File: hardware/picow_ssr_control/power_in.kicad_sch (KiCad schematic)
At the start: 11 parts, among them Q1 IRF4905PBF, Q2 DMG2301L

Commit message: Updated schemas
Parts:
- removed Q2: DMG2301L, Package_TO_SOT_SMD:SOT-23, symbol dragon_mobile:DMG2301L
- REG1: footprint SOT230P700X180-4N -> Package_TO_SOT_SMD:SOT-223; Manufacturer_Name (none) -> Texas Instruments; Manufacturer_Part_Number (none) -> LM7805MPX/NOPB
- RZ1: footprint Resistor_SMD:R_0805_2012Metric -> Resistor_SMD:R_0603_1608Metric
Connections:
- net +VDC renamed VDC
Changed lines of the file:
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@@
   (paper "USLetter")
   (title_block
-    (date "2023-01-27")
+    (date "2023-01-28")
     (rev "0.0.10")
     (comment 2 "http://creativecommons.org/licenses/by-sa/4.0/")

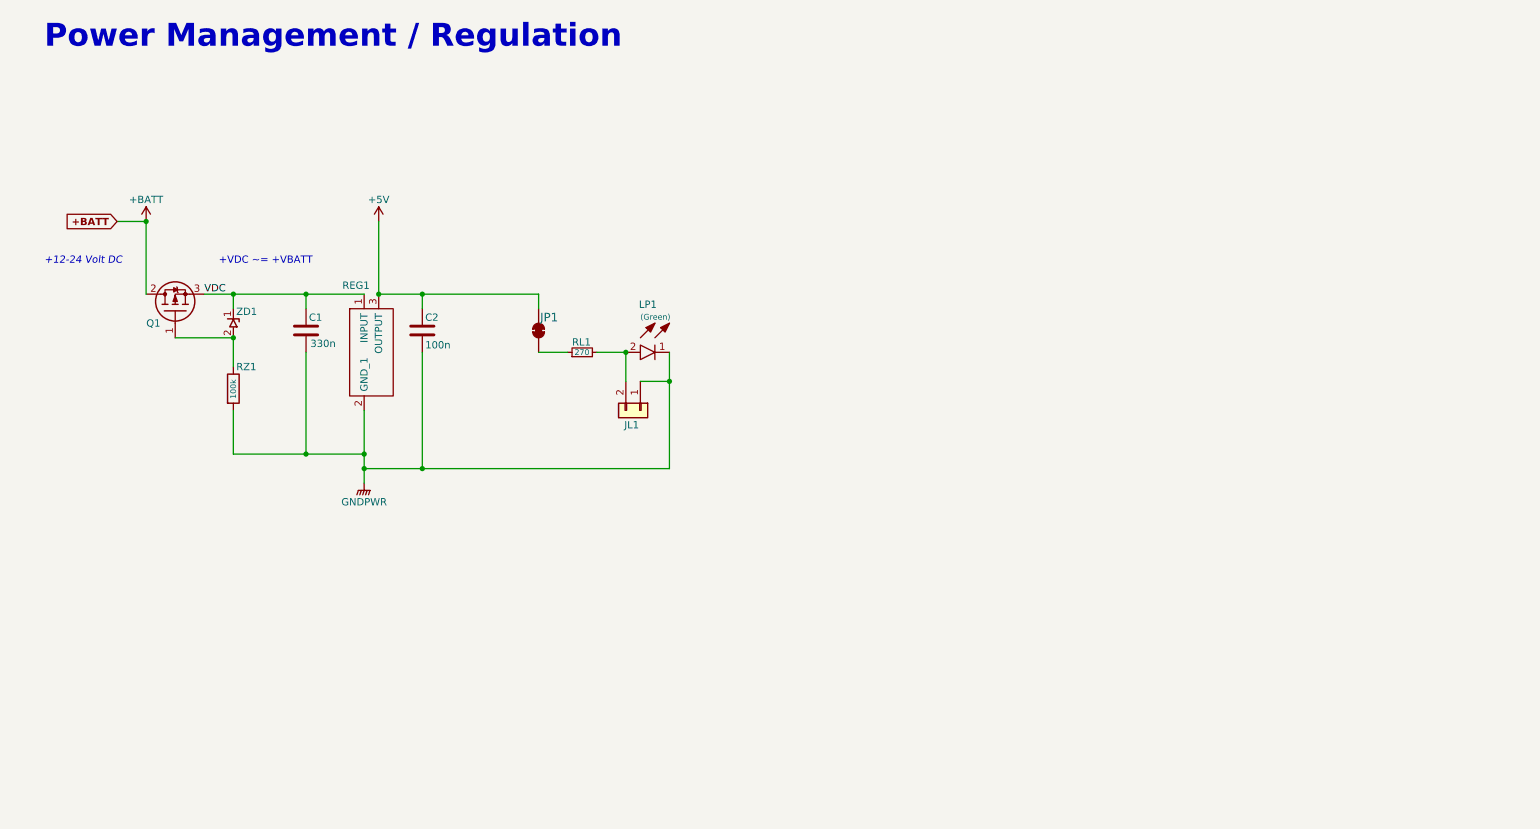
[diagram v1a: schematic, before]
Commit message: Power supply changes plus misc.
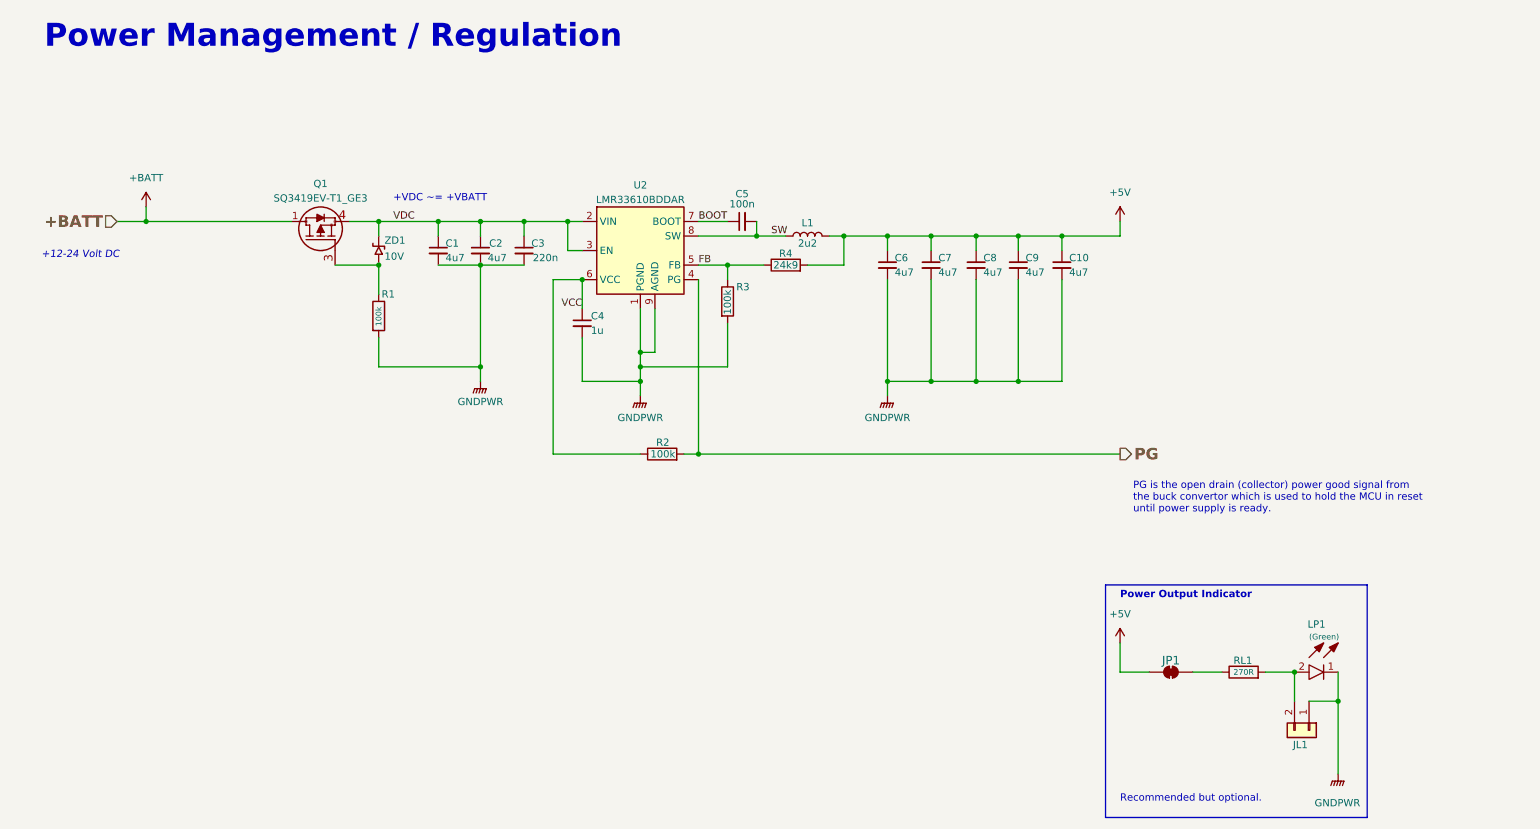
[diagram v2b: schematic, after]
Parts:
- removed C1: 330n, Capacitor_SMD:C_0805_2012Metric, symbol Device:C
- removed C2: 100n, Capacitor_SMD:C_0805_2012Metric, symbol Device:C
- removed Q1: IRF4905PBF, dragon_mobile:TO254P469X1042X1967-3P, symbol dragon_mobile:IRF4905PBF
- removed REG1: LM7805, Package_TO_SOT_SMD:SOT-223, symbol dragon_mobile:LM7805MPX_NOPB
- removed RL1: 270, Resistor_SMD:R_0603_1608Metric, symbol Device:R_Small
- removed RZ1: 100k, Resistor_SMD:R_0603_1608Metric, symbol Device:R
- removed ZD1: +10v Zener Diode, dragon_mobile:BZD27C10P-M3-08, symbol dragon_mobile:BZD27C10P-M3-08
- added C1, C10, C2, C6, C7, C8, C9: 4u7, Capacitor_SMD:C_0805_2012Metric, symbol Device:C_Small
- added C3: 220n, Capacitor_SMD:C_0603_1608Metric, symbol Device:C_Small
- added C4: 1u, Capacitor_SMD:C_0603_1608Metric, symbol Device:C_Small
- added C5: 100n, Capacitor_SMD:C_0603_1608Metric, symbol Device:C_Small
- added L1: 2u2, Inductor_SMD:L_1008_2520Metric, symbol Device:L
- added Q1: SQ3419EV-T1_GE3, dragon_mobile:SOT95P284X110-6N, symbol dragon_mobile:SQ3419EV-T1_BE3
- added R1, R2, R3: 100k, Resistor_SMD:R_0603_1608Metric, symbol Device:R
- added R4: 24k9, Resistor_SMD:R_0603_1608Metric, symbol Device:R
- added RL1: 270R, Resistor_SMD:R_0603_1608Metric, symbol Device:R
- added U2: LMR33610BDDAR, Package_SO:Texas_HSOP-8-1EP_3.9x4.9mm_P1.27mm_ThermalVias, symbol Regulator_Switching:LMR33610BDDAR
- added ZD1: 10V, Diode_SMD:D_0805_2012Metric, symbol dragon_mobile:TSZU52C10
- JL1: footprint Connector_PinHeader_1.00mm:PinHeader_1x02_P1.00mm_Vertical -> dragon_mobile:PinHeader_1x02_P1.00mm_Vertical; Characteristics (none) -> Pin Header; 1mm 1x2 Vertical
- LP1: Manufacturer_Name Lite-On -> (none); Manufacturer_Part_Number LTST-C190KGKT -> (none)
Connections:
- net +5V: now also C10.1, C6.1, C7.1, C8.1, C9.1, L1.2, R4.2
- net +BATT: now also Q1.1 (D), Q1.2 (D), Q1.5 (D), Q1.6 (D)
- net GNDPWR: now also C1.2, C10.2, C2.2, C3.2, C4.2, C6.2, C7.2, C8.2, C9.2, R1.2, R3.2, U2.1 (PGND), U2.9 (AGND)
- net VDC: now also C1.1, C2.1, C3.1, Q1.4 (S), U2.2 (VIN), U2.3 (EN), ZD1.1
- net at JP1.2 (B): now also RL1.1
- net at JL1.2 (Pin_2), LP1.2: now also RL1.2
- new net: Q1.3 (G), R1.1, ZD1.2
- new net BOOT: C5.1, U2.7 (BOOT)
- new net FB: R3.1, R4.1, U2.5 (FB)
- new net PG: R2.2, U2.4 (PG)
- new net SW: C5.2, L1.1, U2.8 (SW)
- new net VCC: C4.1, R2.1, U2.6 (VCC)
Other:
- note added: "PG is the open drain (collector) power good signal from the buck convertor which is used to hold the MCU in reset until power supply is ready."
- note added: "Power Output Indicator"
- note added: "Recommended but optional."

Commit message: Commit before trying changes to power system
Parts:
- LP1: Height 0.8 -> (none)

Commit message: Commit before removing git submodule
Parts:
- added C1: 4u7, Capacitor_SMD:C_0805_2012Metric, symbol Device:C_Small
- added JP1: SolderJumper_2_Bridged, Jumper:SolderJumper-2_P1.3mm_Bridged_RoundedPad1.0x1.5mm, symbol dragon_mobile:SolderJumper_2_Bridged_PowerIn
- added JP2: SolderJumper_2_Open, Jumper:SolderJumper-2_P1.3mm_Open_RoundedPad1.0x1.5mm, symbol Jumper:SolderJumper_2_Open
- added JP3: Conn_01x02, dragon_mobile:PinHeader_1x02_P1.00mm_Vertical, symbol Connector_Generic:Conn_01x02
- L1: symbol Device:L -> dragon_mobile:TFM252012ALVA2R2MTAA
- renumbered C9 to C10, C10 to C11, C1 to C2, C2 to C3, C3 to C4, C4 to C5, C5 to C6, C6 to C7, C7 to C8, C8 to C9, JP1 to JL1, JL1 to JL2
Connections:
- net +BATT: now also JP1.2 (B), JP2.2 (B), JP3.2 (Pin_2)
- net GNDPWR: now also C1.2, JP3.1 (Pin_1)
- net VDC: now also C1.1
- net ZD: now reaches Q1.3 (G), R1.1, ZD1.2
- new net PI1: JP1.1 (A)
- new net PI2: JP2.1 (A)
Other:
- note added: "${SHEETNAME}"
- note removed: "Power Management / Regulation"
- company: (none) -> Michael Cummings
- title: (none) -> Pico W SSR Control
- moved on the sheet: L1, Q1, R1, ZD1
